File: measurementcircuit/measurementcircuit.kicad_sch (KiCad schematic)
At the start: 17 parts, among them J1 Conn_01x05_Socket, J2 Conn_01x05_Socket

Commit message: Only missing POT
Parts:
- removed J1, J2: Conn_01x05_Socket, Connector_Pin:Pin_D1.3mm_L10.0mm_W3.5mm_Flat, symbol Connector:Conn_01x05_Socket
- removed R1, R2, R3, R4, R5: 100 Ω, Resistor_THT:R_Axial_DIN0204_L3.6mm_D1.6mm_P5.08mm_Horizontal, symbol Device:R
- added J1: 2601-3110, Senior_Design:CONN10_2601-3110_WAG, symbol CONN10:2601-3110
- added J10, J11, J12, J8, J9: Conn_01x02, Connector_PinHeader_2.54mm:PinHeader_1x02_P2.54mm_Vertical, symbol Connector_Generic:Conn_01x02
- added J2: 2604-3106, Senior_Design:CONN6_2604-3106_WAG, symbol CONN6:2604-3106
- added J3, J4, J5, J6, J7: 2604-3102, Senior_Design:CONN2_2604-3102_WAG, symbol CONN2:2604-3102
- added RV1, RV2, RV3, RV4, RV5: 1kΩ, Potentiometer_THT:Potentiometer_ACP_CA9-V10_Vertical, symbol Device:R_Potentiometer
- C1, C2, C3, C4, C5: value 10 pF -> 10pF; footprint Capacitor_THT:CP_Axial_L10.0mm_D4.5mm_P15.00mm_Horizontal -> Capacitor_SMD:C_0805_2012Metric
- L1, L2, L3, L4, L5: value 56 μH -> 56μH; footprint Inductor_THT:L_Axial_L5.0mm_D3.6mm_P10.00mm_Horizontal_Murata_BL01RN1A2A2 -> Inductor_SMD:L_0805_2012Metric
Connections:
- net GND: now also RV1.3, RV2.3, RV3.3, RV4.3, RV5.3
- net at L1.1: now also J2.11 (6_1), J2.12 (6_2)
- net at C2.1: now also L1.2, RV1.1; no longer L2.2
- net at L3.1: now also J2.7 (4_1), J2.8 (4_2)
- net at C1.1: now also L2.2, RV2.1; no longer L1.2
- net at C3.1, L3.2: now also RV3.1
- net at C4.1, L4.2: now also RV4.1
- net at C5.1, L5.2: now also RV5.1
- net at L4.1: now also J2.5 (3_1), J2.6 (3_2)
- net at L5.1: now also J2.3 (2_1), J2.4 (2_2)
- net at L2.1: now also J2.10 (5_2), J2.9 (5_1)
- new net: J9.1 (Pin_1), RV2.2
- new net: J4.1 (1_1), J4.2 (1_2), J9.2 (Pin_2)
- new net: J8.1 (Pin_1), RV1.2
- new net: J10.1 (Pin_1), RV3.2
- new net: J11.1 (Pin_1), RV4.2
- new net: J11.2 (Pin_2), J6.1 (1_1), J6.2 (1_2)
- new net: J1.1 (1_1), J1.2 (1_2), J3.4 (2_2)
- new net: J1.10 (5_2), J1.9 (5_1), J5.4 (2_2)
- new net: J1.11 (6_1), J1.12 (6_2), J5.3 (2_1)
- new net: J1.13 (7_1), J1.14 (7_2), J6.4 (2_2)
- new net: J1.15 (8_1), J1.16 (8_2), J6.3 (2_1)
- new net: J1.17 (9_1), J1.18 (9_2), J7.4 (2_2)
- new net: J1.19 (10_1), J1.20 (10_2), J7.3 (2_1)
- new net: J1.3 (2_1), J1.4 (2_2), J3.3 (2_1)
- new net: J1.5 (3_1), J1.6 (3_2), J4.4 (2_2)
- new net: J1.7 (4_1), J1.8 (4_2), J4.3 (2_1)
- new net: J12.2 (Pin_2), J7.1 (1_1), J7.2 (1_2)
- new net: J2.1 (1_1), J2.2 (1_2)
- new net: J12.1 (Pin_1), RV5.2
- new net: J10.2 (Pin_2), J5.1 (1_1), J5.2 (1_2)
- new net: J3.1 (1_1), J3.2 (1_2), J8.2 (Pin_2)

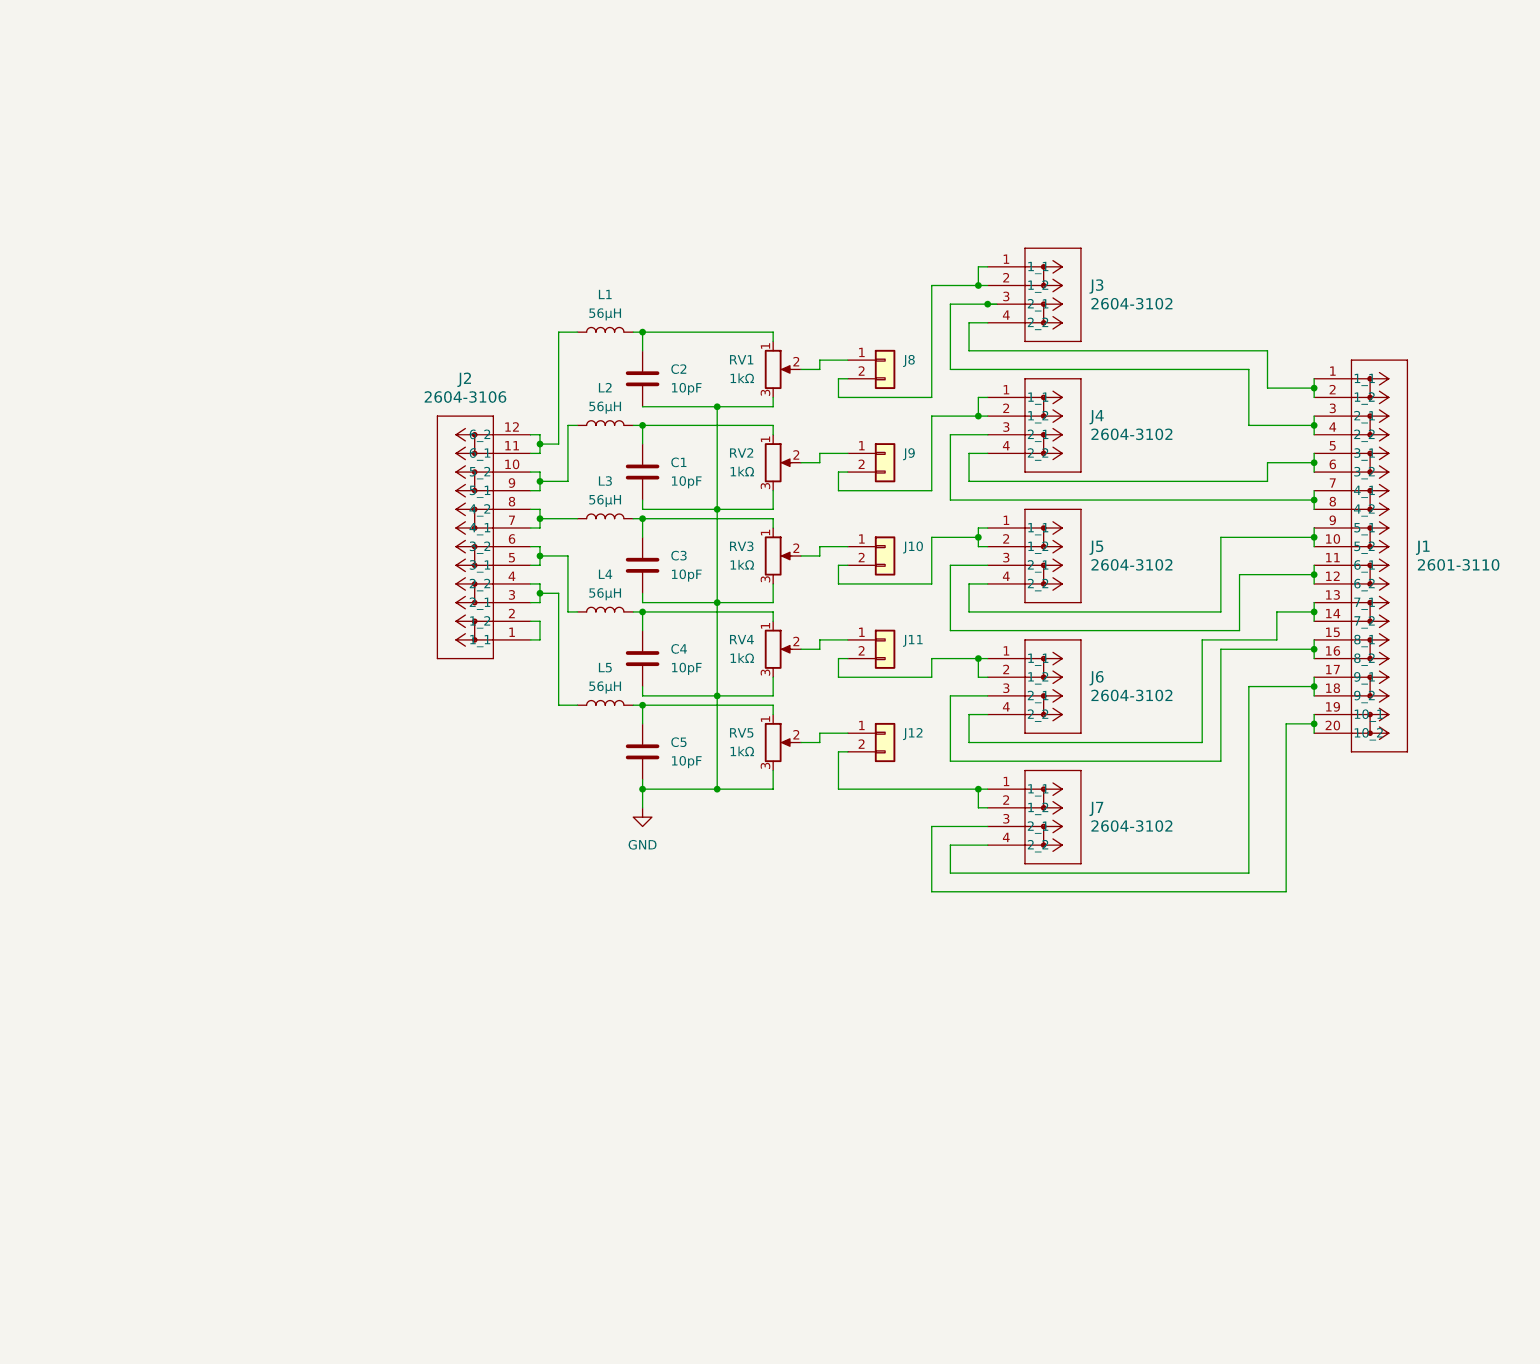
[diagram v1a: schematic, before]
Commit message: Daniel Measurement Circuit Work
Add more routes to make a total of 8 circuits, component selections and placement, routing, finish schematic and pcb design. Switched back to 3 different circuits with shunts. Just need to fix some issues in the Design Rule Check (DRC) caused by the trace width increase aftor placing routes
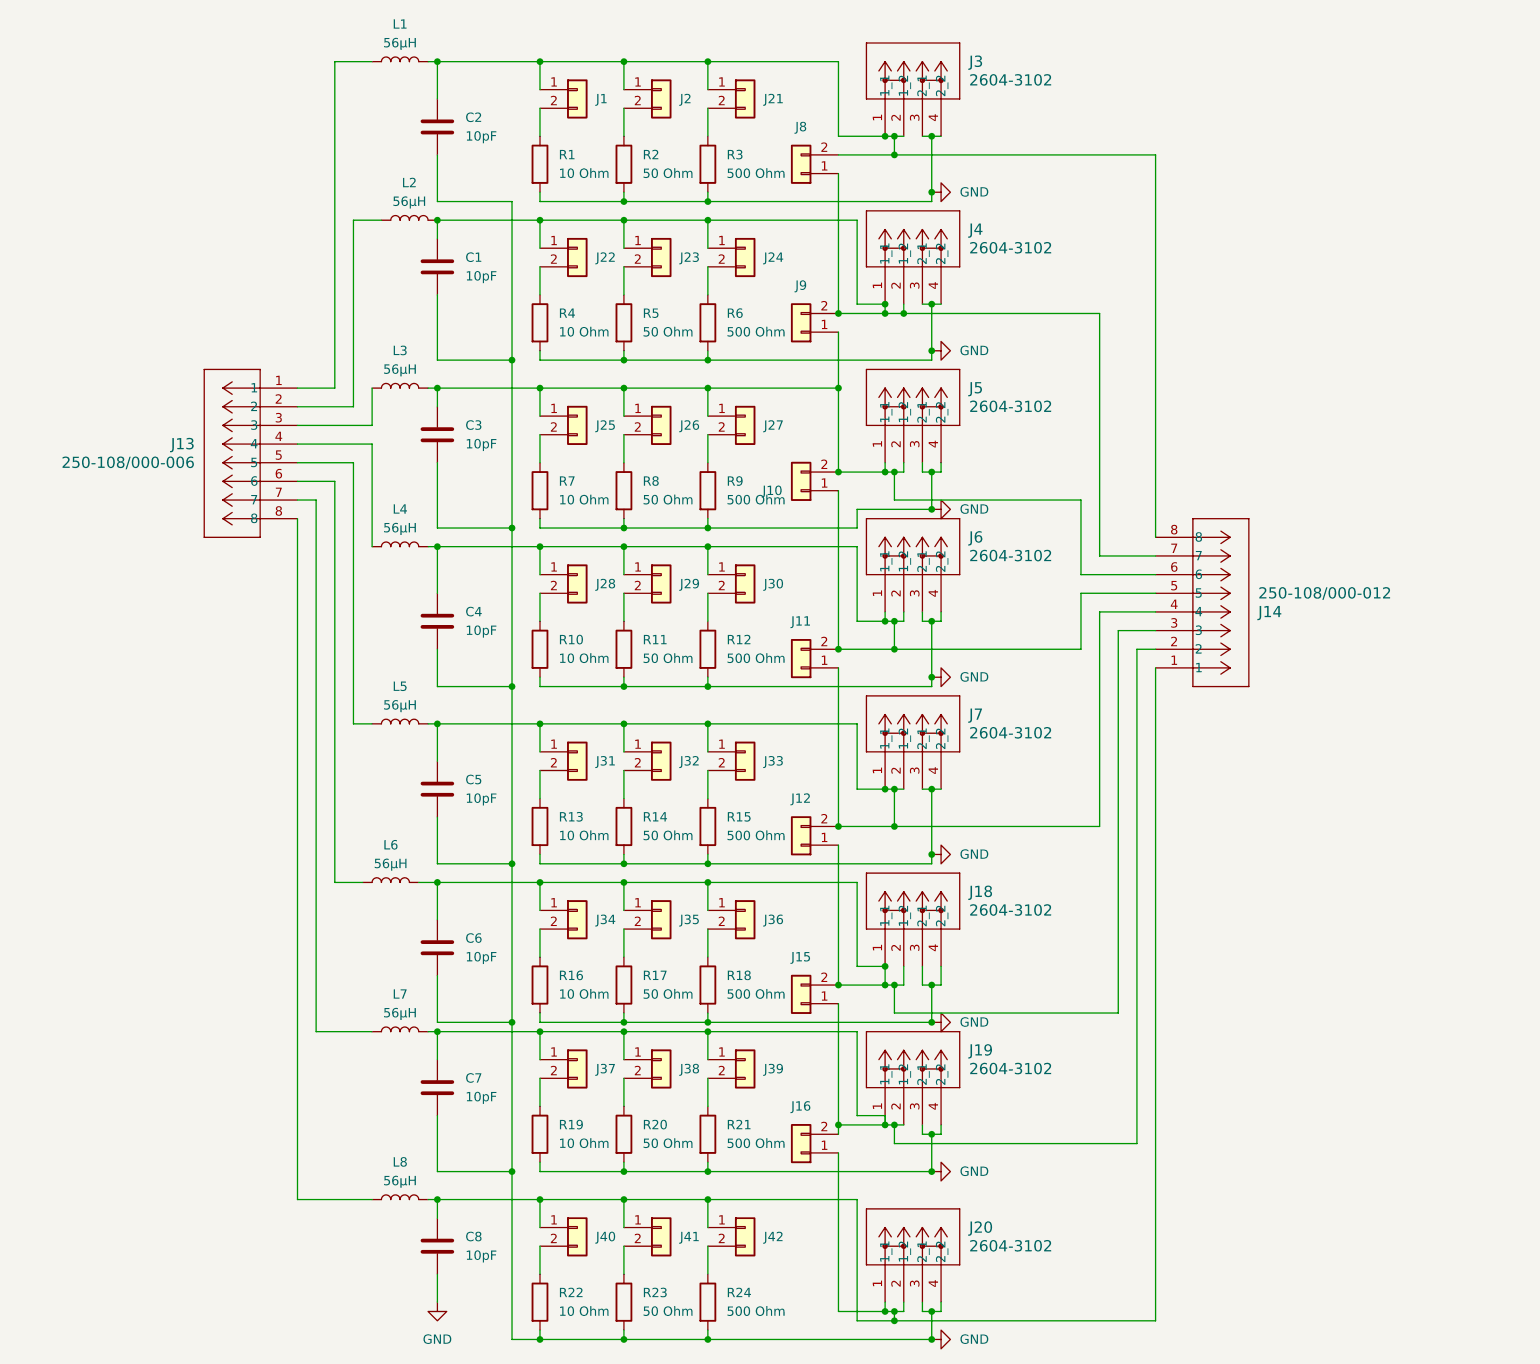
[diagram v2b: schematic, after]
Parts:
- removed J1: 2601-3110, Senior_Design:CONN10_2601-3110_WAG, symbol CONN10:2601-3110
- removed J2: 2604-3106, Senior_Design:CONN6_2604-3106_WAG, symbol CONN6:2604-3106
- removed RV1, RV2, RV3, RV4, RV5: 1kΩ, Potentiometer_THT:Potentiometer_ACP_CA9-V10_Vertical, symbol Device:R_Potentiometer
- added C6, C7, C8: 10pF, Capacitor_SMD:C_0805_2012Metric, symbol Device:C
- added J1, J15, J16, J2, J21, J22, J23, J24, J25, J26, J27, J28, J29, J30, J31, J32, J33, J34, J35, J36, J37, J38, J39, J40, J41, J42: Conn_01x02, Connector_PinHeader_2.54mm:PinHeader_1x02_P2.54mm_Vertical, symbol Connector_Generic:Conn_01x02
- added J13: 250-108/000-006, WAGO_250-108/000-006_connector_BLUE.pretty:CONN8_250-108&slash_000-006_WAG, symbol WAGO_Connectors:250-108_000-006
- added J14: 250-108/000-012, WAGO_250-108/000-012_connector_ORANGE.pretty:CONN8_250-108&slash_000-012_WAG, symbol WAGO_250-108/000-012_connector_ORANGE:250-108_000-012
- added J18, J19, J20: 2604-3102, Wago - 2604-3302_2_pole_connector:CONN2_2604-3302_WAG, symbol CONN2:2604-3102
- added L6, L7, L8: 56μH, Inductor_SMD:L_0805_2012Metric, symbol Device:L
- added R1, R10, R13, R16, R19, R22, R4, R7: 10 Ohm, Resistor_THT:R_Axial_Power_L38.0mm_W9.0mm_P40.64mm, symbol Device:R
- added R11, R14, R17, R2, R20, R23, R5, R8: 50 Ohm, Resistor_THT:R_Axial_Power_L20.0mm_W6.4mm_P25.40mm, symbol Device:R
- added R12, R15, R18, R21, R24, R3, R6, R9: 500 Ohm, Resistor_THT:R_Axial_DIN0309_L9.0mm_D3.2mm_P5.08mm_Vertical, symbol Device:R
- J3, J4, J5, J6, J7: footprint Senior_Design:CONN2_2604-3102_WAG -> Wago - 2604-3302_2_pole_connector:CONN2_2604-3302_WAG
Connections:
- net GND: now also J3.3 (2_1), J3.4 (2_2), J4.3 (2_1), J4.4 (2_2), J5.3 (2_1), J5.4 (2_2), J6.3 (2_1), J6.4 (2_2), J7.3 (2_1), J7.4 (2_2), C6.2, C7.2, C8.2, J18.3 (2_1), J18.4 (2_2), J19.3 (2_1), J19.4 (2_2), J20.3 (2_1), J20.4 (2_2), R1.2, R10.2, R11.2, R12.2, R13.2, R14.2, R15.2, R16.2, R17.2, R18.2, R19.2, R2.2, R20.2, R21.2, R22.2, R23.2, R24.2, R3.2, R4.2, R5.2, R6.2, R7.2, R8.2, R9.2
- net at J9.1 (Pin_1): now also C3.1, J10.2 (Pin_2), J5.1 (1_1), J5.2 (1_2), L3.2, J14.6, J25.1 (Pin_1), J26.1 (Pin_1), J27.1 (Pin_1)
- net at J4.1 (1_1), J4.2 (1_2), J9.2 (Pin_2): now also C1.1, J8.1 (Pin_1), L2.2, J14.7, J22.1 (Pin_1), J23.1 (Pin_1), J24.1 (Pin_1)
- net at L5.1: now also J13.5
- net at C5.1, L5.2: now also J11.1 (Pin_1), J12.2 (Pin_2), J7.1 (1_1), J7.2 (1_2), J14.4, J31.1 (Pin_1), J32.1 (Pin_1), J33.1 (Pin_1)
- net at C2.1, L1.2: now also J3.1 (1_1), J3.2 (1_2), J8.2 (Pin_2), J1.1 (Pin_1), J14.8, J2.1 (Pin_1), J21.1 (Pin_1)
- net at J10.1 (Pin_1): now also C4.1, J11.2 (Pin_2), J6.1 (1_1), J6.2 (1_2), L4.2, J14.5, J28.1 (Pin_1), J29.1 (Pin_1), J30.1 (Pin_1)
- net at L1.1: now also J13.1
- net at L4.1: now also J13.4
- net at L2.1: now also J13.2
- net at L3.1: now also J13.3
- net at J12.1 (Pin_1): now also C6.1, J14.3, J15.2 (Pin_2), J18.1 (1_1), J18.2 (1_2), J34.1 (Pin_1), J35.1 (Pin_1), J36.1 (Pin_1), L6.2
- new net: J42.2 (Pin_2), R24.1
- new net: J36.2 (Pin_2), R18.1
- new net: C8.1, J14.1, J16.1 (Pin_1), J20.1 (1_1), J20.2 (1_2), J40.1 (Pin_1), J41.1 (Pin_1), J42.1 (Pin_1), L8.2
- new net: J40.2 (Pin_2), R22.1
- new net: J30.2 (Pin_2), R12.1
- new net: J1.2 (Pin_2), R1.1
- new net: J41.2 (Pin_2), R23.1
- new net: J25.2 (Pin_2), R7.1
- new net: J29.2 (Pin_2), R11.1
- new net: J21.2 (Pin_2), R3.1
- new net: J31.2 (Pin_2), R13.1
- new net: J23.2 (Pin_2), R5.1
- new net: J34.2 (Pin_2), R16.1
- new net: C7.1, J14.2, J15.1 (Pin_1), J16.2 (Pin_2), J19.1 (1_1), J19.2 (1_2), J37.1 (Pin_1), J38.1 (Pin_1), J39.1 (Pin_1), L7.2
- new net: J37.2 (Pin_2), R19.1
- new net: J32.2 (Pin_2), R14.1
- new net: J26.2 (Pin_2), R8.1
- new net: J2.2 (Pin_2), R2.1
- new net: J28.2 (Pin_2), R10.1
- new net: J33.2 (Pin_2), R15.1
- new net: J38.2 (Pin_2), R20.1
- new net: J24.2 (Pin_2), R6.1
- new net: J13.7, L7.1
- new net: J39.2 (Pin_2), R21.1
- new net: J27.2 (Pin_2), R9.1
- new net: J13.8, L8.1
- new net: J35.2 (Pin_2), R17.1
- new net: J13.6, L6.1
- new net: J22.2 (Pin_2), R4.1
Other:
- moved on the sheet: C1, C2, C3, C4, C5, J10, J11, J12, J3, J4, J5, J6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

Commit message: Update
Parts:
- removed J14: 250-108/000-012, WAGO_250-108/000-012_connector_ORANGE.pretty:CONN8_250-108&slash_000-012_WAG, symbol WAGO_250-108/000-012_connector_ORANGE:250-108_000-012
- added J17: 250-116/000-012, Senior_Design:CONN16_250-116&slash_000-012_WAG, symbol CONN16:250-116_000-012
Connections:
- net GND: no longer J18.3 (2_1), J18.4 (2_2), J19.3 (2_1), J19.4 (2_2), J20.3 (2_1), J20.4 (2_2), J3.3 (2_1), J3.4 (2_2), J4.3 (2_1), J4.4 (2_2), J5.3 (2_1), J5.4 (2_2), J6.3 (2_1), J6.4 (2_2), J7.3 (2_1), J7.4 (2_2), R1.2, R10.2, R11.2, R12.2, R13.2, R14.2, R15.2, R16.2, R17.2, R18.2, R19.2, R2.2, R20.2, R21.2, R22.2, R23.2, R24.2, R3.2, R4.2, R5.2, R6.2, R7.2, R8.2, R9.2
- net at J16.1 (Pin_1), J20.1 (1_1), J20.2 (1_2)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: now also J17.16; no longer C8.1, L8.2
- net at J10.2 (Pin_2), J25.1 (Pin_1), J26.1 (Pin_1)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: now also J17.6; no longer C3.1, L3.2
- net at C1.1, J22.1 (Pin_1), J23.1 (Pin_1)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: now also R4.2, R5.2, R6.2, J17.3, J17.4
- net at J1.1 (Pin_1), J2.1 (Pin_1), J21.1 (Pin_1)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: now also J17.2; no longer C2.1, L1.2
- net at C4.1, J10.1 (Pin_1), J11.2 (Pin_2)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: now also R10.2, R11.2, R12.2, J17.7, J17.8
- net at J11.1 (Pin_1), J12.2 (Pin_2), J31.1 (Pin_1)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: now also J17.10; no longer C5.1, L5.2
- net at J12.1 (Pin_1), J15.2 (Pin_2), J18.1 (1_1)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: now also J17.12; no longer C6.1, L6.2
- net at J15.1 (Pin_1), J16.2 (Pin_2), J19.1 (1_1)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: now also J17.14; no longer C7.1, L7.2
- new net: C8.1, J17.15, L8.2, R22.2, R23.2, R24.2
- new net: C6.1, J17.11, L6.2, R16.2, R17.2, R18.2
- new net: C3.1, J17.5, L3.2, R7.2, R8.2, R9.2
- new net: C2.1, J17.1, L1.2, R1.2, R2.2, R3.2
- new net: C5.1, J17.9, L5.2, R13.2, R14.2, R15.2
- new net: C7.1, J17.13, L7.2, R19.2, R20.2, R21.2
- new net: J20.3 (2_1), J20.4 (2_2)
- new net: J18.3 (2_1), J18.4 (2_2)
- new net: J7.3 (2_1), J7.4 (2_2)
- new net: J19.3 (2_1), J19.4 (2_2)
- new net: J5.3 (2_1), J5.4 (2_2)
- new net: J4.3 (2_1), J4.4 (2_2)
- new net: J3.3 (2_1), J3.4 (2_2)
- new net: J6.3 (2_1), J6.4 (2_2)

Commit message: Fix traces after rearrangement of measurement schematic
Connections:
- net GND: now also J18.3 (2_1), J18.4 (2_2), J19.3 (2_1), J19.4 (2_2), J20.3 (2_1), J20.4 (2_2), J3.3 (2_1), J3.4 (2_2), J4.3 (2_1), J4.4 (2_2), J5.3 (2_1), J5.4 (2_2), J6.3 (2_1), J6.4 (2_2), J7.3 (2_1), J7.4 (2_2)

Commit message: Resize canvas
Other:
- title: (none) -> Measurement Circuit
- moved on the sheet: C1, C2, C3, C4, C5, C6, C7, C8, J1, J10, J11, J12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

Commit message: update before new design work
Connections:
- net at C1.1, J17.3, J17.4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: no longer J22.1 (Pin_1), J23.1 (Pin_1), J24.1 (Pin_1), J8.1 (Pin_1)
- net at C4.1, J11.2 (Pin_2), J17.7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: no longer J10.1 (Pin_1), J28.1 (Pin_1), J29.1 (Pin_1), J30.1 (Pin_1)
- new net: J10.1 (Pin_1), J28.1 (Pin_1), J29.1 (Pin_1), J30.1 (Pin_1)
- new net: J22.1 (Pin_1), J23.1 (Pin_1), J24.1 (Pin_1), J8.1 (Pin_1)
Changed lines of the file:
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@@
 	)
 	(junction
-		(at 125.73 69.85)
-		(diameter 0)
-		(color 0 0 0 0)
-	)
-	(junction
 		(at 81.28 204.47)
 		(diameter 0)
@@
 	)
 	(junction
-		(at 125.73 114.3)
-		(diameter 0)
-		(color 0 0 0 0)
-	)
-	(junction
 		(at 96.52 158.75)
 		(diameter 0)
@@
 	(wire
 		(pts
-			(xy 125.73 71.12) (xy 125.73 69.85)
-		)
-		(stroke
-			(width 0)
-			(type default)
-		)
-	)
-	(wire
-		(pts
 			(xy 132.08 193.04) (xy 132.08 195.58)
 		)
@@
 	(wire
 		(pts
-			(xy 81.28 114.3) (xy 125.73 114.3)
+			(xy 81.28 114.3) (xy 128.27 114.3)
 		)
 		(stroke
@@
 	(wire
 		(pts
-			(xy 125.73 69.85) (xy 128.27 69.85)
-		)
-		(stroke
-			(width 0)
-			(type default)
-		)
-	)
-	(wire
-		(pts
 			(xy 85.09 135.89) (xy 96.52 135.89)
 		)
@@
 	(wire
 		(pts
-			(xy 81.28 69.85) (xy 125.73 69.85)
+			(xy 81.28 69.85) (xy 128.27 69.85)
 		)
 		(stroke
@@
 	(wire
 		(pts
-			(xy 125.73 63.5) (xy 125.73 69.85)
+			(xy 125.73 63.5) (xy 125.73 71.12)
 		)
 		(stroke
@@
 	(wire
 		(pts
-			(xy 125.73 114.3) (xy 128.27 114.3)
-		)
-		(stroke
-			(width 0)
-			(type default)
-		)
-	)
-	(wire
-		(pts
 			(xy 168.91 132.08) (xy 177.8 132.08)
 		)
@@
 	(wire
 		(pts
-			(xy 125.73 106.68) (xy 125.73 114.3)
+			(xy 125.73 106.68) (xy 125.73 115.57)
 		)
 		(stroke
@@
 		)
 		(stroke
-			(width 0)
-			(type default)
-		)
-	)
-	(wire
-		(pts
-			(xy 125.73 115.57) (xy 125.73 114.3)
-		)
-		(stroke
